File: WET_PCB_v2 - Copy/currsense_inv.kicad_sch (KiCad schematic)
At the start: 9 parts, among them J17 Capacitor connector, U1 Opamp_Quad

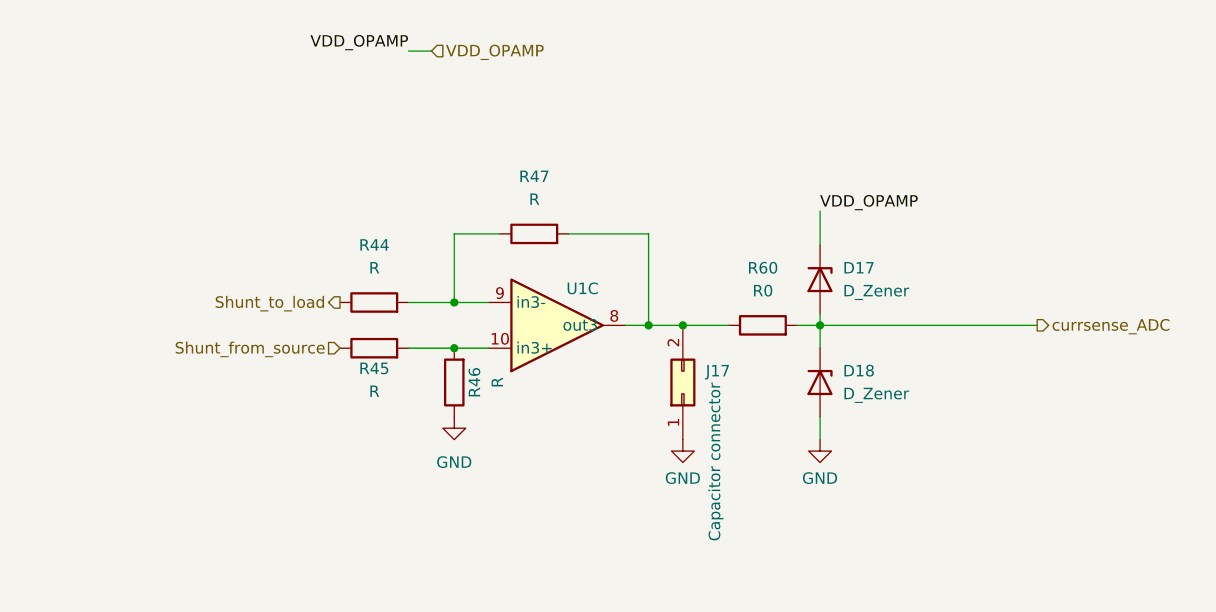
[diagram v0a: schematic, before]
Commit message: microcontroller to chip traces done
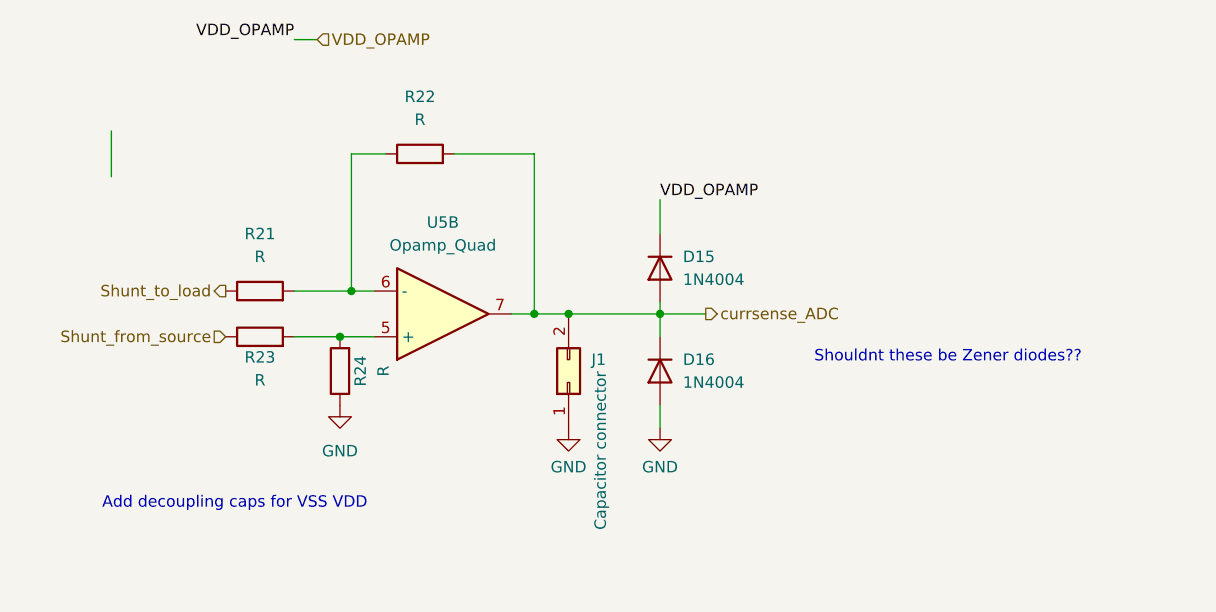
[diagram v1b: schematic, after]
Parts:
- removed D17, D18: D_Zener, Diode_SMD:D_SMF, symbol Device:D_Zener
- removed J17: Capacitor connector, Connector_PinSocket_2.54mm:PinSocket_1x02_P2.54mm_Horizontal, symbol Connector_Generic:Conn_02x01
- removed R44, R45, R46, R47: R, Resistor_SMD:R_0805_2012Metric_Pad1.20x1.40mm_HandSolder, symbol Device:R
- removed R60: R0, Resistor_SMD:R_0805_2012Metric_Pad1.20x1.40mm_HandSolder, symbol Device:R
- removed U1: Opamp_Quad, Package_DIP:DIP-14_W7.62mm, symbol Device:Opamp_Quad
- added D15, D16: 1N4004, Diode_THT:D_DO-41_SOD81_P10.16mm_Horizontal, symbol Diode:1N4004
- added J1: Capacitor connector, symbol Connector_Generic:Conn_02x01
- added R21, R22, R23, R24: R, symbol Device:R
- added U5: Opamp_Quad, symbol Device:Opamp_Quad
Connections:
- net GND: now also D16.2 (A), J1.1 (Pin_1), R24.1
- net Shunt_from_source: now also R23.1
- net Shunt_to_load: now also R21.1
- net VDD_OPAMP: now also D15.1 (K)
- net currsense_ADC: now also D15.2 (A), D16.1 (K), J1.2 (Pin_2), R22.2, U5.7
- new net: R21.2, R22.1, U5.6 (-)
- new net: R23.2, R24.2, U5.5 (+)
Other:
- note added: "Add decoupling caps for VSS VDD"
- note added: "Shouldnt these be Zener diodes??"
